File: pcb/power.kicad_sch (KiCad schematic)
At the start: 14 parts, among them J13 Power, J2 USB_C_USB2.0_16P, U2 LM66200DRLR, U3 USBLC6-2P6, U5 LD1117S33TR_SOT223

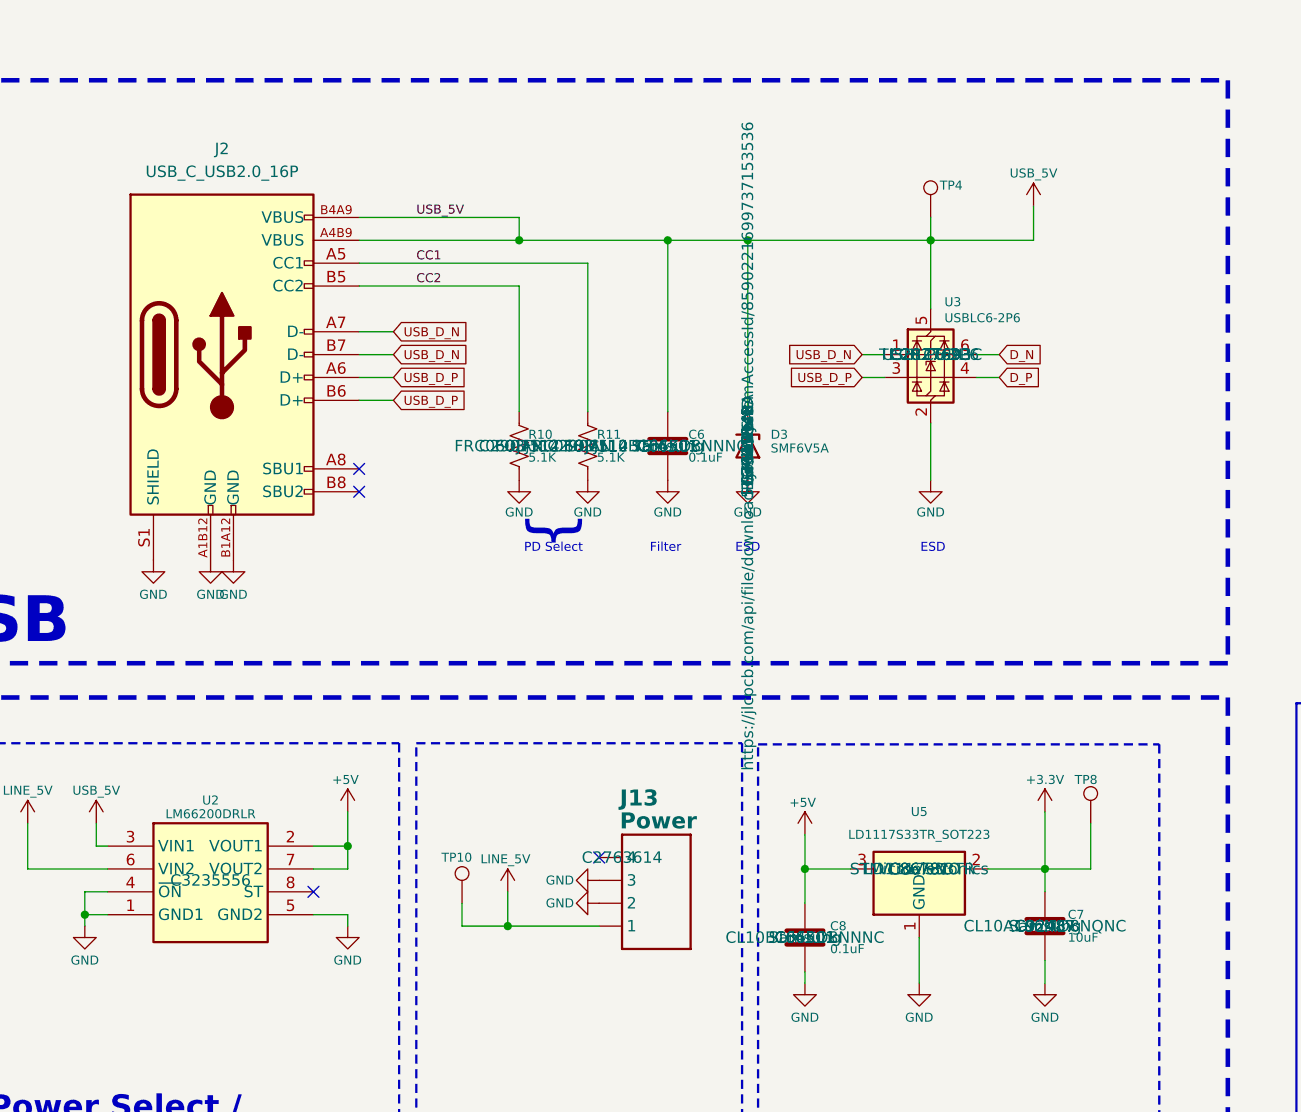
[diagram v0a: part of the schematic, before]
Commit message: Changed SPI to 8 pin connector
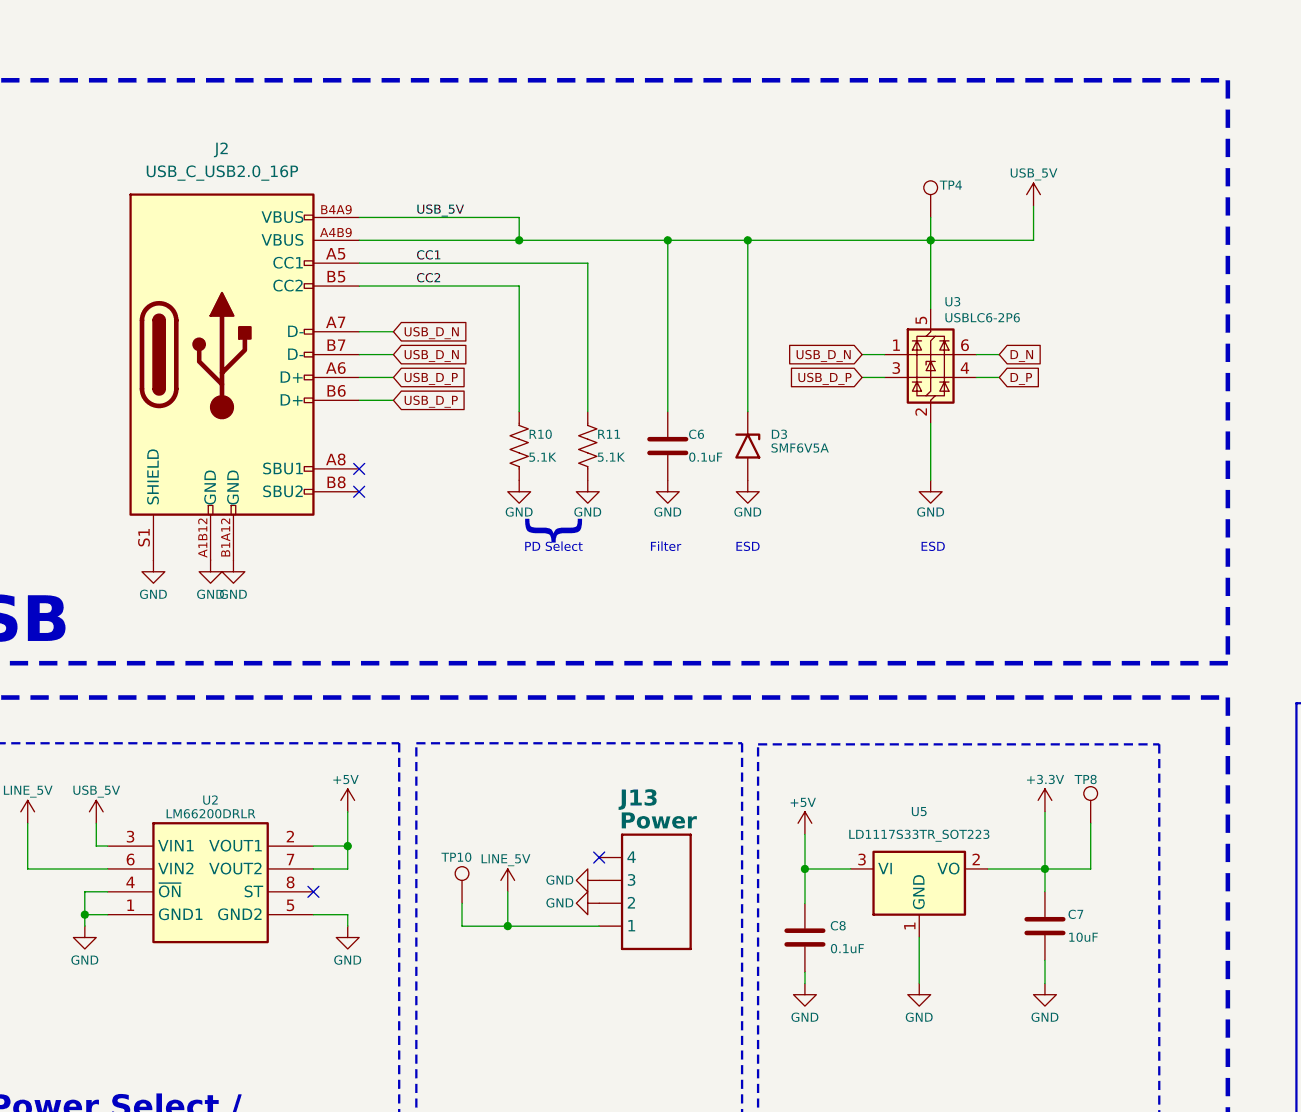
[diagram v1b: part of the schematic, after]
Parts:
- TP10, TP4, TP8: now in the parts list
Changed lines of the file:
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@@
 					(size 1.27 1.27)
 				)
+				(hide yes)
 			)
 		)
@@
 					(size 1.27 1.27)
 				)
+				(hide yes)
 			)
 		)
@@
 					(size 1.27 1.27)
 				)
+				(hide yes)
 			)
 		)
@@
 					(size 1.27 1.27)
 				)
+				(hide yes)
 			)
 		)
@@
 		(unit 1)
 		(exclude_from_sim no)
-		(in_bom no)
+		(in_bom yes)
 		(on_board yes)
 		(dnp no)
@@
 		(unit 1)
 		(exclude_from_sim no)
-		(in_bom no)
+		(in_bom yes)
 		(on_board yes)
 		(dnp no)
@@
 					(size 1.27 1.27)
 				)
+				(hide yes)
 			)
 		)
@@
 					(size 1.27 1.27)
 				)
+				(hide yes)
 			)
 		)
@@
 					(size 1.27 1.27)
 				)
+				(hide yes)
 			)
 		)
@@
 					(size 1.27 1.27)
 				)
+				(hide yes)
 			)
 		)
@@
 					(size 1.27 1.27)
 				)
+				(hide yes)
 			)
 		)
@@
 					(size 1.27 1.27)
 				)
+				(hide yes)
 			)
 		)
@@
 					(size 1.27 1.27)
 				)
+				(hide yes)
 			)
 		)
@@
 					(size 1.27 1.27)
 				)
+				(hide yes)
 			)
 		)
@@
 					(size 1.27 1.27)
 				)
+				(hide yes)
 			)
 		)
@@
 					(size 1.27 1.27)
 				)
+				(hide yes)
 			)
 		)
@@
 					(size 1.27 1.27)
 				)
+				(hide yes)
 			)
 		)
@@
 					(size 1.27 1.27)
 				)
+				(hide yes)
 			)
 		)
@@
 					(size 1.27 1.27)
 				)
+				(hide yes)
 			)
 		)
@@
 					(size 1.27 1.27)
 				)
+				(hide yes)
 			)
 		)
@@
 					(size 1.27 1.27)
 				)
+				(hide yes)
 			)
 		)
@@
 					(size 1.27 1.27)
 				)
+				(hide yes)
 			)
 		)
@@
 					(size 1.27 1.27)
 				)
+				(hide yes)
 			)
 		)
@@
 					(size 1.27 1.27)
 				)
+				(hide yes)
 			)
 		)
@@
 					(size 1.27 1.27)
 				)
+				(hide yes)
 			)
 		)
@@
 					(size 1.27 1.27)
 				)
+				(hide yes)
 			)
 		)
@@
 					(size 1.27 1.27)
 				)
+				(hide yes)
 			)
 		)
@@
 					(size 1.27 1.27)
 				)
+				(hide yes)
 			)
 		)
@@
 					(size 1.27 1.27)
 				)
+				(hide yes)
 			)
 		)
@@
 		(unit 1)
 		(exclude_from_sim no)
-		(in_bom no)
+		(in_bom yes)
 		(on_board yes)
 		(dnp no)
@@
 					(size 1.27 1.27)
 				)
+				(hide yes)
 			)
 		)
@@
 					(size 1.27 1.27)
 				)
+				(hide yes)
 			)
 		)
@@
 					(size 1.27 1.27)
 				)
+				(hide yes)
 			)
 		)
@@
 					(size 1.27 1.27)
 				)
+				(hide yes)
 			)
 		)
@@
 					(size 1.27 1.27)
 				)
+				(hide yes)
 			)
 		)
@@
 					(size 1.27 1.27)
 				)
+				(hide yes)
 			)
 		)
@@
 					(size 1.27 1.27)
 				)
+				(hide yes)
 			)
 		)
@@
 					(size 1.27 1.27)
 				)
-			)
-		)
+				(hide yes)
+			)
+		)

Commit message: added open hw; changed test points; added pulls on buttons
change buttons to be 2 connectors with pull ups.
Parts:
- TP10, TP4, TP8: footprint TestPoint:TestPoint_Pad_D1.0mm -> CRGM Mechanical:TestPoint_Pad_D1.0mm
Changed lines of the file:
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@@
 			)
 		)
-		(property "Footprint" "TestPoint:TestPoint_Pad_D1.0mm"
+		(property "Footprint" "CRGM Mechanical:TestPoint_Pad_D1.0mm"
 			(at 160.02 102.87 0)
 			(effects
@@
 			)
 		)
-		(property "Footprint" "TestPoint:TestPoint_Pad_D1.0mm"
+		(property "Footprint" "CRGM Mechanical:TestPoint_Pad_D1.0mm"
 			(at 90.17 111.76 0)
 			(effects
@@
 			)
 		)
-		(property "Footprint" "TestPoint:TestPoint_Pad_D1.0mm"
+		(property "Footprint" "CRGM Mechanical:TestPoint_Pad_D1.0mm"
 			(at 142.24 35.56 0)
 			(effects

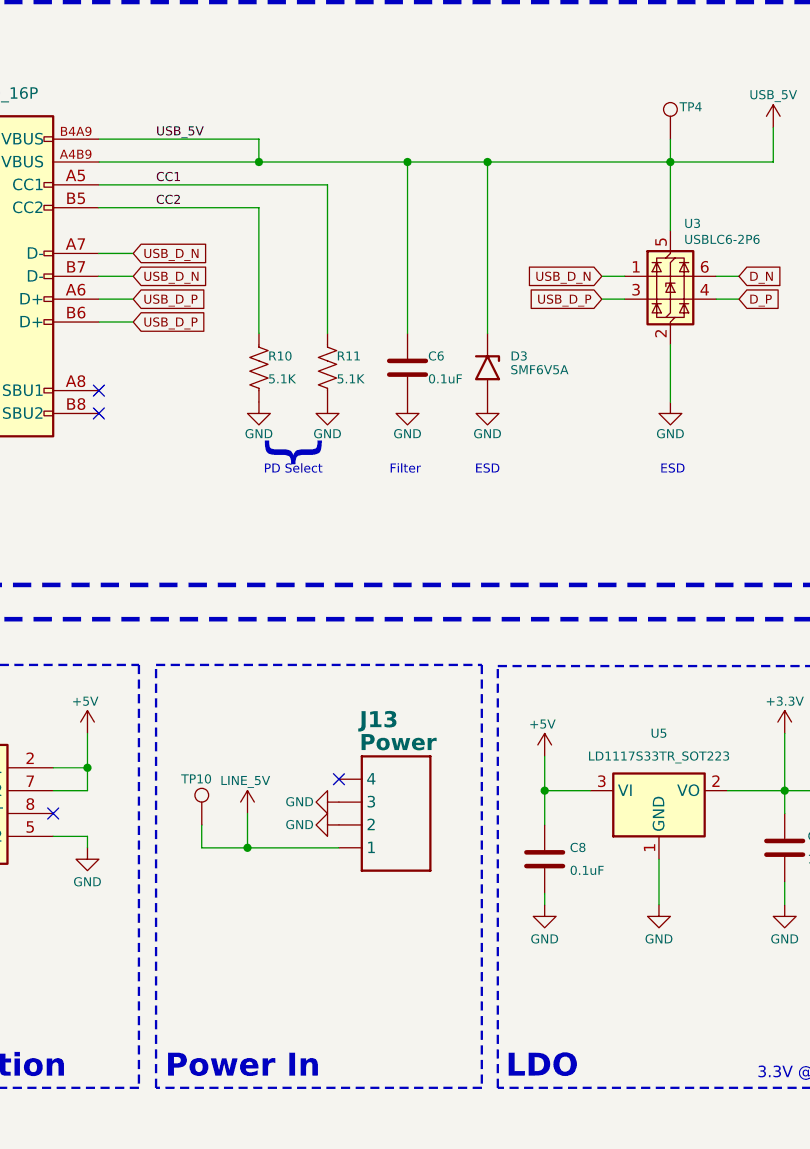
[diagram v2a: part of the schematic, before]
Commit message: Change panel to be 1x1
Changed connectors be vertical rather than horizontal.
Updated TVS diodes to DFN1006 rather than SMF
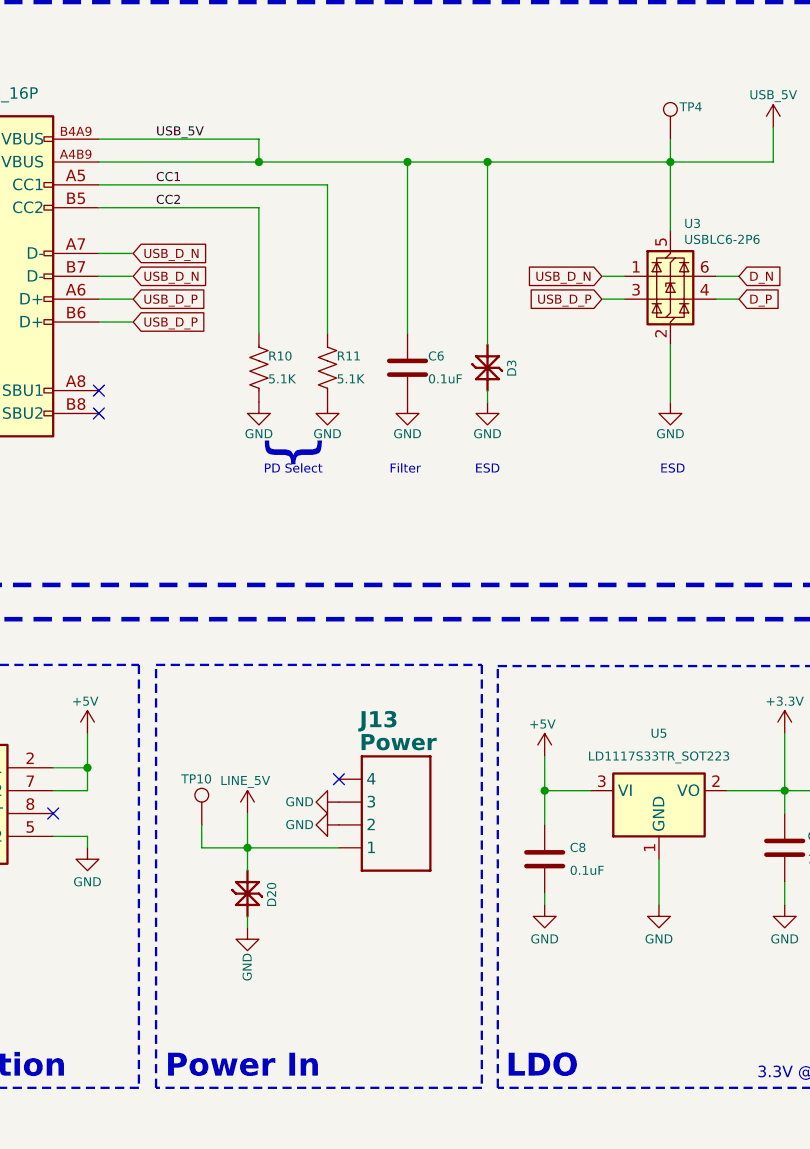
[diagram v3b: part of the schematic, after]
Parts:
- removed D3: SMF6V5A, CRGM Passive:D_SOD-123F, symbol Diode:SMF6V5A
- added D20, D3: PESD5V5C1BL, CRGM Passive:DFN1006-2, symbol CRGM Passive:PESD5V5C1BLYL
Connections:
- net GND: now also D20.1 (K1), D3.1 (K1)
- net LINE_5V: now also D20.2 (K2)
- net USB_5V: now also D3.2 (K2)

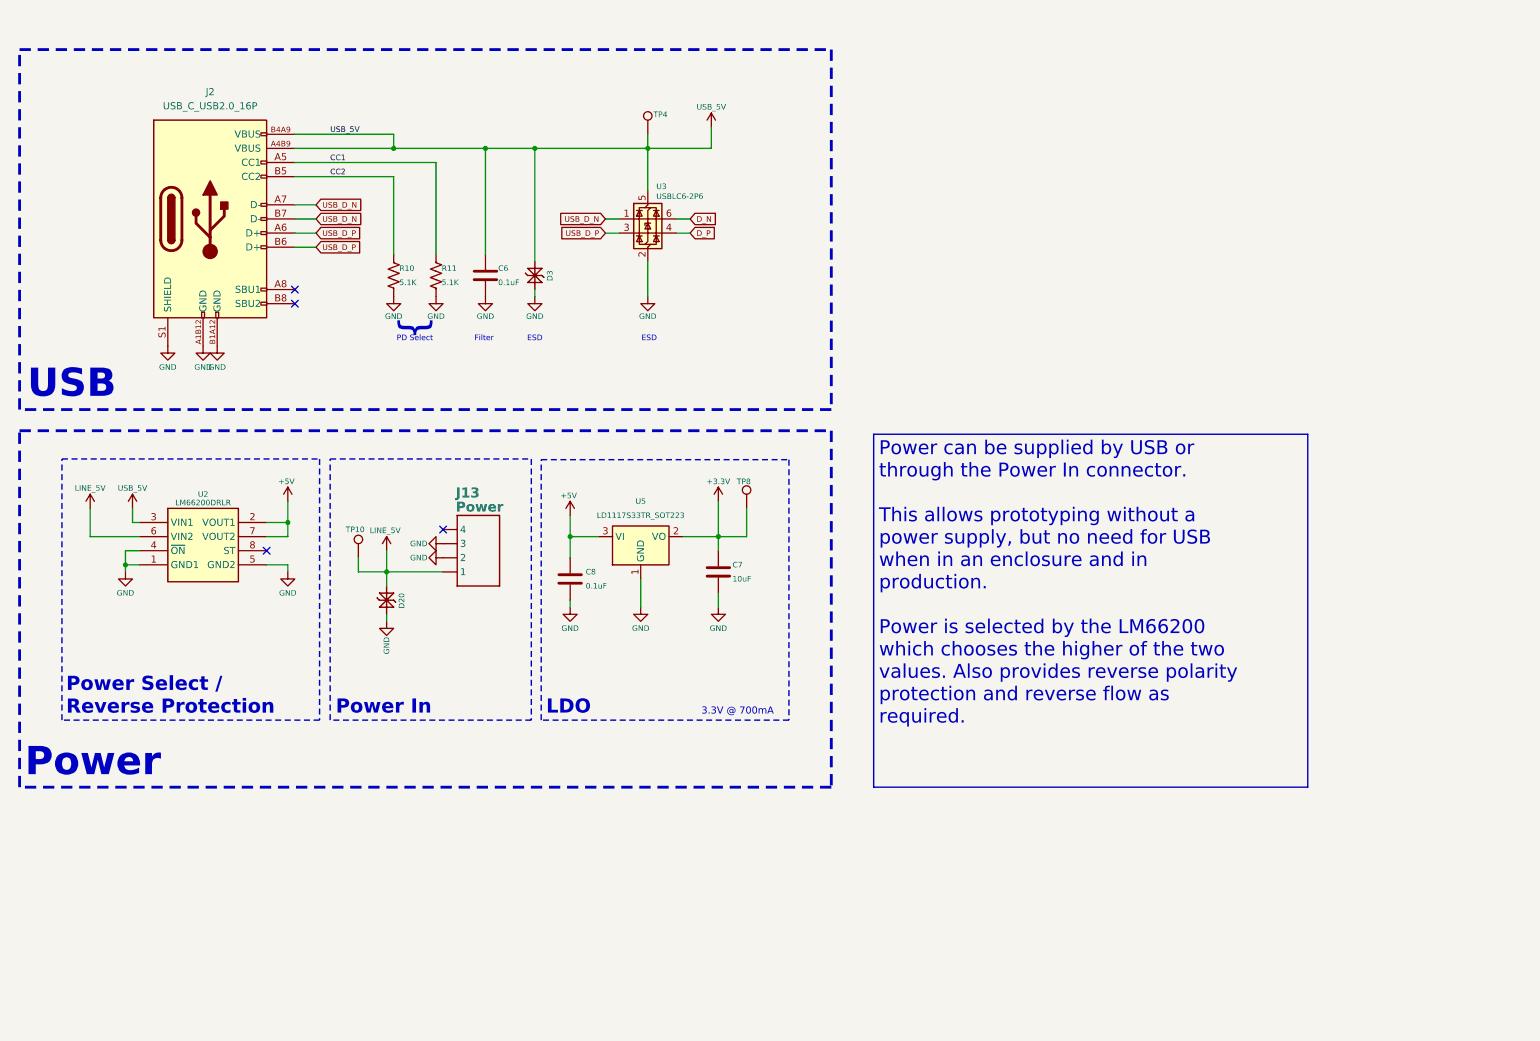
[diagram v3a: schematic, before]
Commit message: Major overhaul of IO
Added GPIO module
Added SPI interface
Added serial interface
Added power selection
Added power LEDs
Changed v3.3 LDO
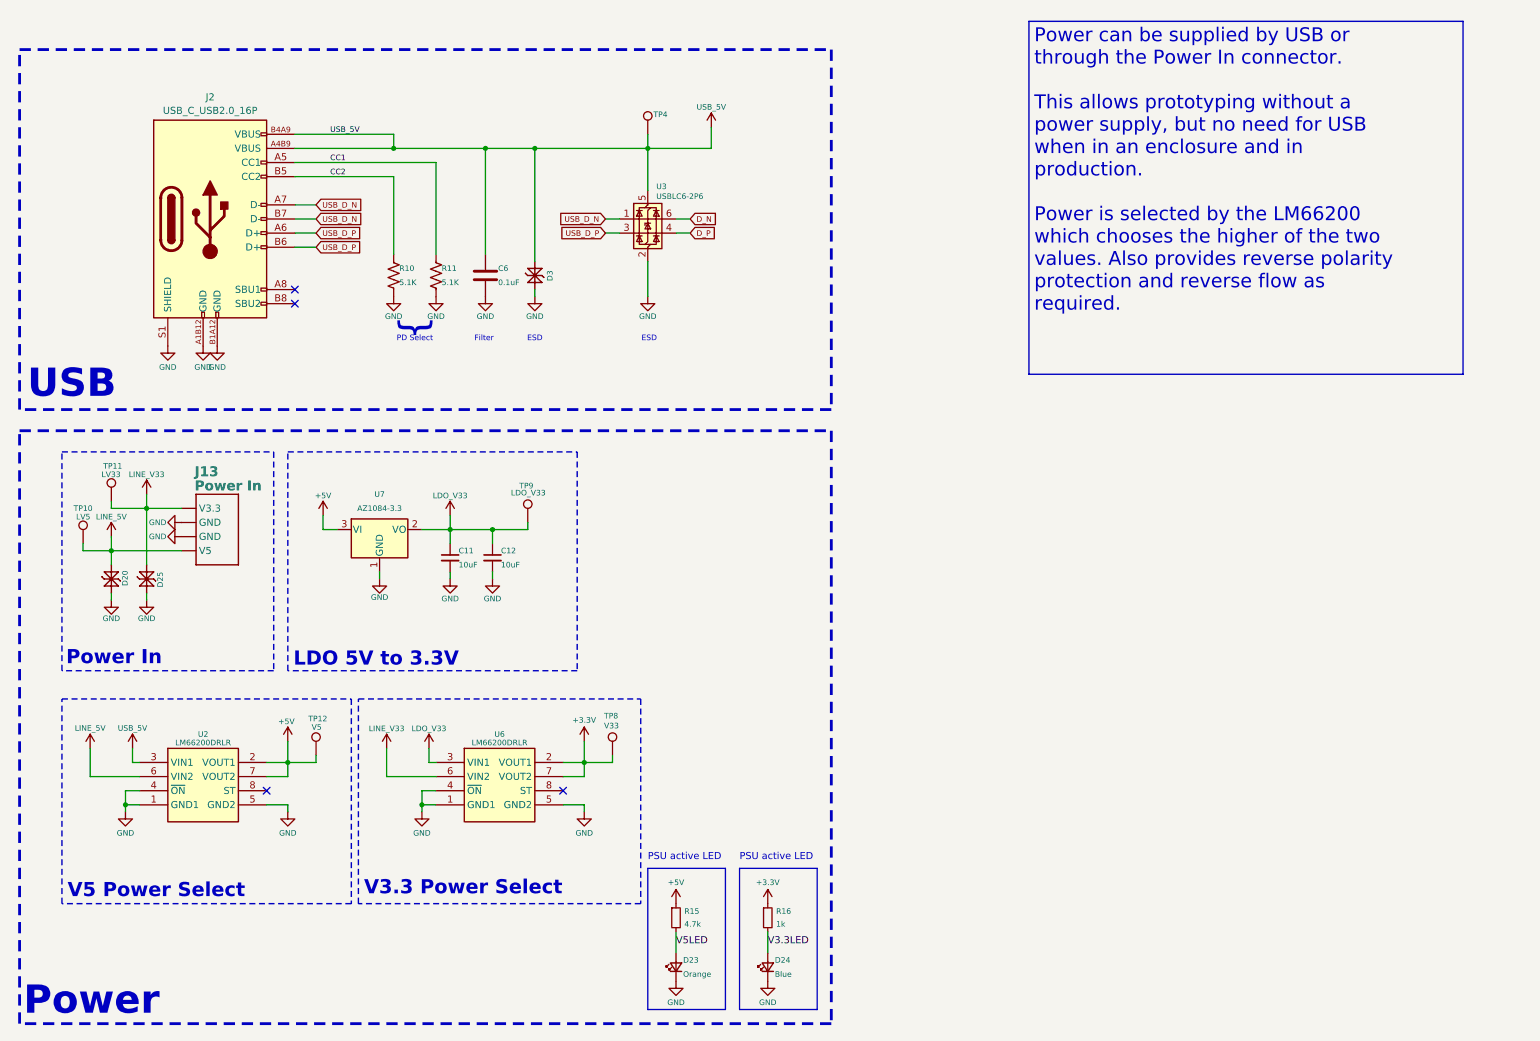
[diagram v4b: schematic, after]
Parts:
- removed C7: 10uF, Capacitor_SMD:C_0603_1608Metric, symbol Device:C
- removed C8: 0.1uF, Capacitor_SMD:C_0603_1608Metric, symbol Device:C
- removed U5: LD1117S33TR_SOT223, Package_TO_SOT_SMD:SOT-223-3_TabPin2, symbol Regulator_Linear:LD1117S33TR_SOT223
- added C11, C12: 10uF, Capacitor_SMD:C_0603_1608Metric, symbol Device:C_Small
- added D23: Orange, CRGM Passive:LED_0603_1608Metric, symbol Device:LED_Small
- added D24: Blue, CRGM Passive:LED_0603_1608Metric, symbol Device:LED_Small
- added D25: PESD3V3S1BL, CRGM Passive:DFN1006-2, symbol CRGM Passive:PESD3V3S1BL
- added R15: 4.7k, Resistor_SMD:R_0603_1608Metric, symbol Device:R_Small
- added R16: 1k, Resistor_SMD:R_0603_1608Metric, symbol Device:R_Small
- added TP11: LV33, CRGM Mechanical:TestPoint_Pad_D1.0mm, symbol Connector:TestPoint
- added TP12: V5, TestPoint:TestPoint_Pad_D1.0mm, symbol Connector:TestPoint
- added TP9: LDO_V33, TestPoint:TestPoint_Pad_D1.0mm, symbol Connector:TestPoint
- added U6: LM66200DRLR, CRGM Power:SOTFL50P160X60-8N, symbol CRGM Power:LM66200DRLR
- added U7: AZ1084-3.3, CRGM Power:TO-252-2, symbol CRGM Power:AZ1084-3.3
- J13: value Power -> Power In; symbol CRGM Connector:JST-SH-4 -> CRGM Connector:AQ_POWER; Digikey (none) -> 455-BM04B-SRSS-TBTR-ND; LCSC_PN C2763614 -> (none); MPN SM04B-SRSS-TB -> BM04B-SRSS-TBT(LF)(SN); Mouser (none) -> 306-BM04BSRSSTBTLFSN
- TP10: value VLINE -> LV5
- TP8: footprint CRGM Mechanical:TestPoint_Pad_D1.0mm -> TestPoint:TestPoint_Pad_D1.0mm; now left out of the parts list
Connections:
- net +3.3V: now also R16.1, U6.2 (VOUT1), U6.7 (VOUT2)
- net +5V: now also R15.1, TP12.1, U7.3 (VI)
- net GND: now also C11.2, C12.2, D23.1 (K), D24.1 (K), D25.1 (K1), U6.1 (GND1), U6.4 (~{ON}), U6.5 (GND2), U7.1 (GND)
- net LINE_V33: now reaches J13.4 (V3.3)
- net LINE_V33: now also D25.2 (K2), TP11.1, U6.6 (VIN2)
- new net LDO_V33: C11.1, C12.1, TP9.1, U6.3 (VIN1), U7.2 (VO)
- new net V3.3LED: D24.2 (A), R16.2
- new net V5LED: D23.2 (A), R15.2
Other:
- note added: "LDO 5V to 3.3V"
- note added: "PSU active LED"
- note added: "V3.3 Power Select"
- note added: "V5 Power Select"
- note removed: "3.3V @ 700mA"
- note removed: "LDO"
- note removed: "Power Select / Reverse Protection"
- moved on the sheet: D20, J13, TP10, U2
